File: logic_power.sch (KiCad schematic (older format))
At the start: 28 parts

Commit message: Huge schematic and documentation update
Signed-off-by: Patrick Rudolph <siro@das-labor.org>
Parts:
- removed C?: 2u2, symbol Device:C_Small
- removed D?: 6V8, symbol Device:D_Zener_Small
- removed D?: D_Schottky, symbol Device:D_Schottky
- removed Q?: MMBTA42, symbol Device:Q_NPN_BCE
- removed R?: 220k, symbol Device:R
- removed R?: 130, symbol Device:R
- removed T?: PA1528, symbol Device:Transformer_1P_2S
- added C? (x2): 10u, symbol Device:C_Small
- added D?: MBR2H200SF, Diode_SMD:D_SOD-123, symbol Device:D_Schottky
- added D?: BAT54T1G, Diode_SMD:D_SOD-123, symbol Device:D_Schottky
- added TR?: 7491199212, symbol Transformer:TRANSF6
- C?: value 100p -> 360p
- D?: value 8V1 -> BZT52B8V2; footprint (none) -> Diode_SMD:D_SOD-123
- D?: value D_Schottky -> BAT54T1G; footprint (none) -> Diode_SMD:D_SOD-123
- R?: value 68 -> 300k
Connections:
- net 12V: now also D?.1 (K)
- net 12V+_isolated: now also C?.1, C?.1
- net 12V-_isolated: now also C?.2, C?.2, TR?.7
- net GND: now also TR?.4, TR?.5; no longer C?.2
- net V_IN: now also C?.1, R?.2, TR?.1
- net at Q?.1 (D): now also D?.2 (A), TR?.2; no longer R?.2
- net at D?.2 (A): now also TR?.8
- net at R?.1: now also C?.2, D?.1 (K); no longer C?.1
- net V_BACKUP renamed V_SUPPLY
- new net: D?.2 (A), TR?.3, TR?.6
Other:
- note added: "Coutmin = (Ioutmax * 10) / (fsw * Vout_ripple)\n= (0,05A * 10) / (200e3 * 0,1)\n= 25uF"
- note added: "Csnub = (2 * Lleak * Ip ^2 * n ^2 ) / (Vout ^2)\n= (2 * 2.3e-6 * 0.32^2 * 0.33^2) / (12^2)\n= 356pF"
- note added: "Rclamp = (4 * Vr^2) / (Lleak * Ip ^2 * fsw)\n= 4 * 60^2 / (2.3e-6 * 0.32^2 * 200e3)\n= 14.4 / (2.3e-6 * 0.32^2 * 200)\n= 305k"
- note added: "Vin 20-60V\nN 1:0.29\nVout 12V\nIpri = 0.32A\nIsec = 0.100A\nLleak = 2.3 uH"
- moved on the sheet: C?, R?

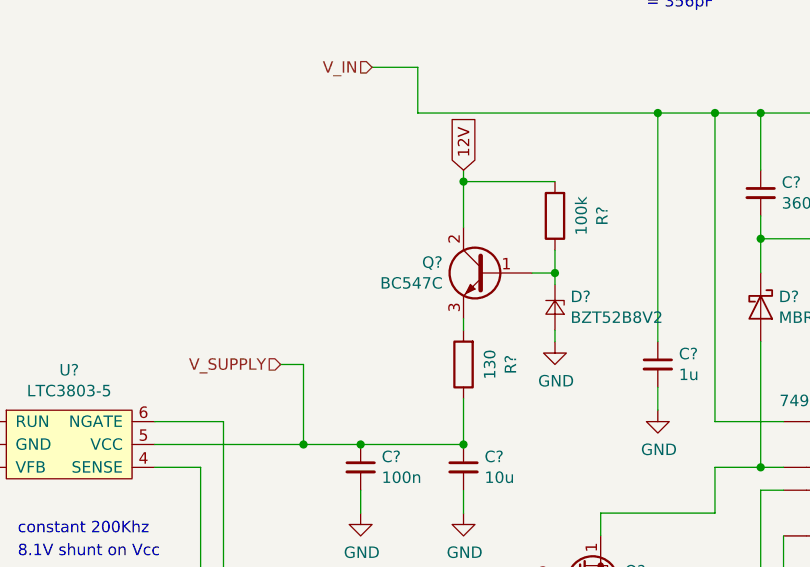
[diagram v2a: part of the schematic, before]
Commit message: Add more packages
Signed-off-by: Patrick Rudolph <siro@das-labor.org>
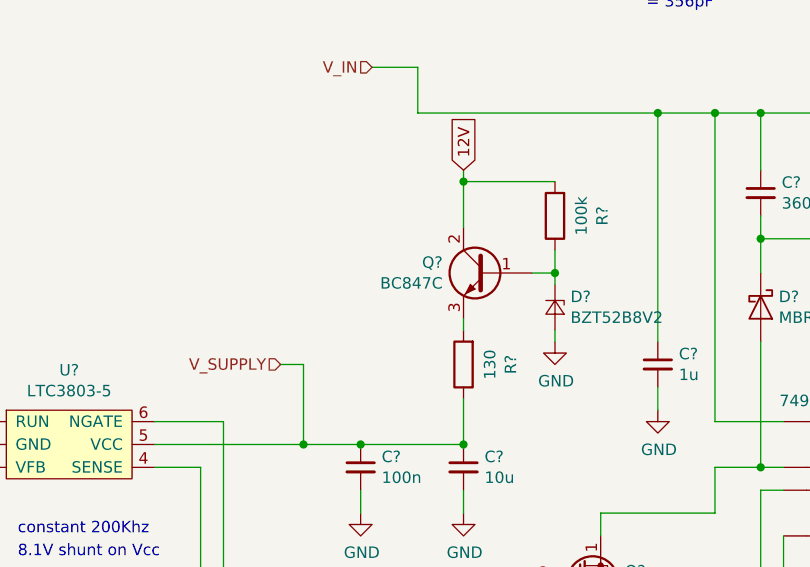
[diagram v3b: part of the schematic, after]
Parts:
- C? (x6): footprint (none) -> Capacitor_SMD:C_1206_3216Metric
- C? (x3): footprint (none) -> Capacitor_SMD:C_0603_1608Metric
- Q?: value BC547C -> BC847C; footprint (none) -> Package_TO_SOT_SMD:SOT-23
- R? (x6): footprint (none) -> Resistor_SMD:R_0603_1608Metric
- U?: footprint (none) -> Package_TO_SOT_SMD:SOT-23-6_Handsoldering
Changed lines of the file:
@@
 EESchema Schematic File Version 4
 LIBS:mppt_power-cache
-EELAYER 29 0
+EELAYER 30 0
 EELAYER END
 $Descr A4 11693 8268
@@
 F 0 "U?" H 3275 4025 50  0000 C CNN
 F 1 "LTC3803-5" H 3275 3934 50  0000 C CNN
-F 2 "" H 3250 3500 50  0001 C CNN
+F 2 "Package_TO_SOT_SMD:SOT-23-6_Handsoldering" H 3250 3500 50  0001 C CNN
 F 3 "https://www.analog.com/media/en/technical-documentation/data-sheets/38035fc.pdf" H 3250 3500 50  0001 C CNN
 	1    3250 3500
@@
 F 0 "C?" H 5092 3446 50  0000 L CNN
 F 1 "10u" H 5092 3355 50  0000 L CNN
-F 2 "" H 5000 3400 50  0001 C CNN
+F 2 "Capacitor_SMD:C_1206_3216Metric" H 5000 3400 50  0001 C CNN
 F 3 "~" H 5000 3400 50  0001 C CNN
 	1    5000 3400
@@
 F 0 "C?" H 4642 3446 50  0000 L CNN
 F 1 "100n" H 4642 3355 50  0000 L CNN
-F 2 "" H 4550 3400 50  0001 C CNN
+F 2 "Capacitor_SMD:C_0603_1608Metric" H 4550 3400 50  0001 C CNN
 F 3 "~" H 4550 3400 50  0001 C CNN
 	1    4550 3400
@@
 F 0 "R?" V 6493 2150 50  0000 C CNN
 F 1 "300k" V 6584 2150 50  0000 C CNN
-F 2 "" V 6630 2150 50  0001 C CNN
+F 2 "Resistor_SMD:R_0603_1608Metric" V 6630 2150 50  0001 C CNN
 F 3 "~" H 6700 2150 50  0001 C CNN
 	1    6700 2150
@@
 F 0 "C?" H 6392 2246 50  0000 L CNN
 F 1 "360p" H 6392 2155 50  0000 L CNN
-F 2 "" H 6300 2200 50  0001 C CNN
+F 2 "Capacitor_SMD:C_0603_1608Metric" H 6300 2200 50  0001 C CNN
 F 3 "~" H 6300 2200 50  0001 C CNN
 	1    6300 2200
@@
 F 0 "R?" V 4743 4150 50  0000 C CNN
 F 1 "4k7" V 4834 4150 50  0000 C CNN
-F 2 "" V 4880 4150 50  0001 C CNN
+F 2 "Resistor_SMD:R_0603_1608Metric" V 4880 4150 50  0001 C CNN
 F 3 "~" H 4950 4150 50  0001 C CNN
 	1    4950 4150
@@
 F 0 "C?" H 7692 3796 50  0000 L CNN
 F 1 "10u" H 7692 3705 50  0000 L CNN
-F 2 "" H 7600 3750 50  0001 C CNN
+F 2 "Capacitor_SMD:C_1206_3216Metric" H 7600 3750 50  0001 C CNN
 F 3 "~" H 7600 3750 50  0001 C CNN
 	1    7600 3750
@@
 F 0 "C?" H 8042 3796 50  0000 L CNN
 F 1 "10u" H 8042 3705 50  0000 L CNN
-F 2 "" H 7950 3750 50  0001 C CNN
+F 2 "Capacitor_SMD:C_1206_3216Metric" H 7950 3750 50  0001 C CNN
 F 3 "~" H 7950 3750 50  0001 C CNN
 	1    7950 3750
@@
 F 0 "C?" H 5942 2996 50  0000 L CNN
 F 1 "1u" H 5942 2905 50  0000 L CNN
-F 2 "" H 5850 2950 50  0001 C CNN
+F 2 "Capacitor_SMD:C_1206_3216Metric" H 5850 2950 50  0001 C CNN
 F 3 "~" H 5850 2950 50  0001 C CNN
 	1    5850 2950
@@
 F 0 "R?" V 7543 2800 50  0000 C CNN
 F 1 "680" V 7634 2800 50  0000 C CNN
-F 2 "" V 7680 2800 50  0001 C CNN
+F 2 "Resistor_SMD:R_0603_1608Metric" V 7680 2800 50  0001 C CNN
 F 3 "~" H 7750 2800 50  0001 C CNN
 	1    7750 2800
@@
 F 0 "C?" H 2142 3446 50  0000 L CNN
 F 1 "1n" H 2142 3355 50  0000 L CNN
-F 2 "" H 2050 3400 50  0001 C CNN
+F 2 "Capacitor_SMD:C_0603_1608Metric" H 2050 3400 50  0001 C CNN
 F 3 "~" H 2050 3400 50  0001 C CNN
 	1    2050 3400
@@
 F 0 "R?" V 2193 3200 50  0000 C CNN
 F 1 "22k" V 2284 3200 50  0000 C CNN
-F 2 "" V 2330 3200 50  0001 C CNN
+F 2 "Resistor_SMD:R_0603_1608Metric" V 2330 3200 50  0001 C CNN
 F 3 "~" H 2400 3200 50  0001 C CNN
 	1    2400 3200
@@
 P 5100 2550
 F 0 "Q?" H 5291 2596 50  0000 L CNN
-F 1 "BC547C" H 5291 2505 50  0000 L CNN
-F 2 "" H 5300 2650 50  0001 C CNN
+F 1 "BC847C" H 5291 2505 50  0000 L CNN
+F 2 "Package_TO_SOT_SMD:SOT-23" H 5300 2650 50  0001 C CNN
 F 3 "~" H 5100 2550 50  0001 C CNN
 	1    5100 2550
@@
 F 0 "R?" V 4793 2950 50  0000 C CNN
 F 1 "130" V 4884 2950 50  0000 C CNN
-F 2 "" V 4930 2950 50  0001 C CNN
+F 2 "Resistor_SMD:R_0603_1608Metric" V 4930 2950 50  0001 C CNN
 F 3 "~" H 5000 2950 50  0001 C CNN
 	1    5000 2950
@@
 F 0 "R?" V 5193 2300 50  0000 C CNN
 F 1 "100k" V 5284 2300 50  0000 C CNN
-F 2 "" V 5330 2300 50  0001 C CNN
+F 2 "Resistor_SMD:R_0603_1608Metric" V 5330 2300 50  0001 C CNN
 F 3 "~" H 5400 2300 50  0001 C CNN
 	1    5400 2300
@@
 F 0 "C?" H 8542 2796 50  0000 L CNN
 F 1 "10u" H 8542 2705 50  0000 L CNN
-F 2 "" H 8450 2750 50  0001 C CNN
+F 2 "Capacitor_SMD:C_1206_3216Metric" H 8450 2750 50  0001 C CNN
 F 3 "~" H 8450 2750 50  0001 C CNN
 	1    8450 2750
@@
 F 0 "C?" H 8192 2796 50  0000 L CNN
 F 1 "10u" H 8192 2705 50  0000 L CNN
-F 2 "" H 8100 2750 50  0001 C CNN
+F 2 "Capacitor_SMD:C_1206_3216Metric" H 8100 2750 50  0001 C CNN
 F 3 "~" H 8100 2750 50  0001 C CNN
 	1    8100 2750

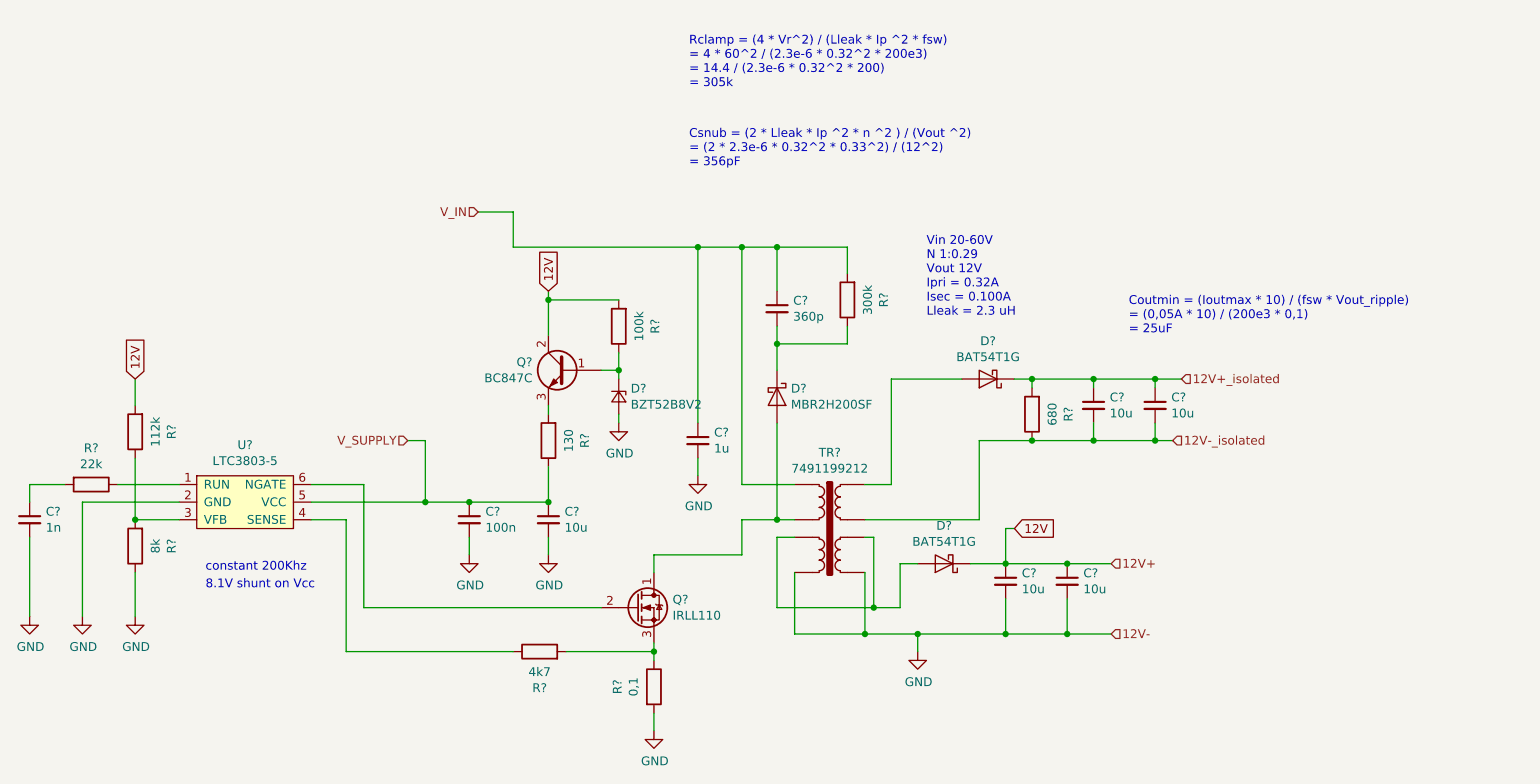
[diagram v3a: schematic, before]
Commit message: Split into more schematics, add more comments
Signed-off-by: Patrick Rudolph <siro@das-labor.org>
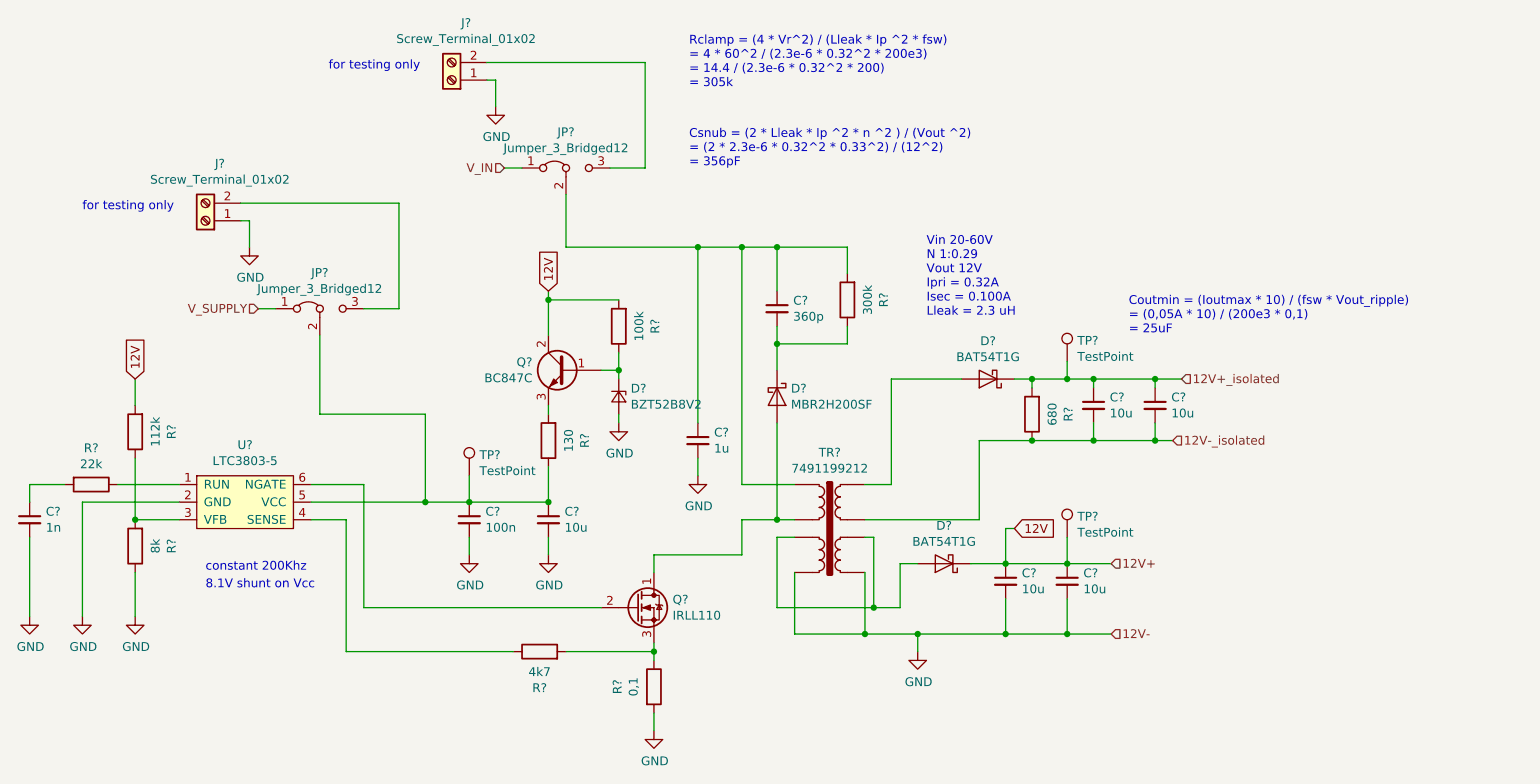
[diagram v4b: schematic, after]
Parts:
- added J? (x2): Screw_Terminal_01x02, symbol Connector:Screw_Terminal_01x02
- added JP? (x2): Jumper_3_Bridged12, symbol Jumper:Jumper_3_Bridged12
- added TP? (x3): TestPoint, symbol Connector:TestPoint
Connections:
- net 12V: now also TP?.1
- net 12V+_isolated: now also TP?.1
- net GND: now also J?.1 (Pin_1), J?.1 (Pin_1)
- net V_IN: now also JP?.1 (A); no longer C?.1, C?.1, R?.2, TR?.1
- net V_SUPPLY: now also JP?.1 (A); no longer C?.1, C?.1, R?.1, U?.5 (VCC)
- new net: C?.1, C?.1, JP?.2 (C), R?.2, TR?.1
- new net: C?.1, C?.1, JP?.2 (C), R?.1, TP?.1, U?.5 (VCC)
- new net: J?.2 (Pin_2), JP?.3 (B) (x2)
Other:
- note added: "for testing only"
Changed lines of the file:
@@
 $Descr A4 11693 8268
 encoding utf-8
-Sheet 2 3
+Sheet 2 5
 Title ""
 Date ""
@@
 Wire Wire Line
 	2350 3300 2350 3950
-Wire Wire Line
-	3650 3300 4300 3300
 Wire Wire Line
 	4550 3300 5000 3300
@@
 	7750 2650 7750 2600
 Connection ~ 7750 2600
-Text HLabel 4600 1650 0    50   Input ~ 0
+Text HLabel 4750 1400 0    50   Input ~ 0
 V_IN
-Wire Wire Line
-	4600 1650 4800 1650
-Wire Wire Line
-	4800 1650 4800 1850
-Wire Wire Line
-	4800 1850 5850 1850
 $Comp
 L Device:R R?
@@
 $EndComp
 Wire Wire Line
-	7750 2600 8100 2600
+	7750 2600 7950 2600
 Wire Wire Line
 	7750 2950 8100 2950
@@
 	-1   0    0    1
 $EndComp
-Text HLabel 4200 2950 0    50   Input ~ 0
+Text HLabel 3350 2200 0    50   Input ~ 0
 V_SUPPLY
-Wire Wire Line
-	4200 2950 4300 2950
-Wire Wire Line
-	4300 2950 4300 3300
+$Comp
+L Connector:TestPoint TP?
+U 1 1 5DA4B3AA
+P 4550 3150
+F 0 "TP?" H 4608 3268 50  0000 L CNN
+F 1 "TestPoint" H 4608 3177 50  0000 L CNN
+F 2 "" H 4750 3150 50  0001 C CNN
+F 3 "~" H 4750 3150 50  0001 C CNN
+	1    4550 3150
+	1    0    0    -1
+$EndComp
+$Comp
+L Connector:TestPoint TP?
+U 1 1 5DA4BF3C
+P 7950 3500
+F 0 "TP?" H 8008 3618 50  0000 L CNN
+F 1 "TestPoint" H 8008 3527 50  0000 L CNN
+F 2 "" H 8150 3500 50  0001 C CNN
+F 3 "~" H 8150 3500 50  0001 C CNN
+	1    7950 3500
+	1    0    0    -1
+$EndComp
+Wire Wire Line
+	7950 3500 7950 3650
+$Comp
+L Connector:TestPoint TP?
+U 1 1 5DA503D9
+P 7950 2500
+F 0 "TP?" H 8008 2618 50  0000 L CNN
+F 1 "TestPoint" H 8008 2527 50  0000 L CNN
+F 2 "" H 8150 2500 50  0001 C CNN
+F 3 "~" H 8150 2500 50  0001 C CNN
+	1    7950 2500
+	1    0    0    -1
+$EndComp
+Wire Wire Line
+	7950 2500 7950 2600
+Connection ~ 7950 2600
+Wire Wire Line
+	7950 2600 8100 2600
+Wire Wire Line
+	4550 3150 4550 3300
+$Comp
+L Jumper:Jumper_3_Bridged12 JP?
+U 1 1 5DA5817D
+P 3700 2200
+F 0 "JP?" H 3700 2404 50  0000 C CNN
+F 1 "Jumper_3_Bridged12" H 3700 2313 50  0000 C CNN
+F 2 "" H 3700 2200 50  0001 C CNN
+F 3 "~" H 3700 2200 50  0001 C CNN
+	1    3700 2200
+	1    0    0    -1
+$EndComp
+Wire Wire Line
+	3650 3300 4300 3300
+Wire Wire Line
+	3350 2200 3450 2200
+Wire Wire Line
+	3700 2350 3700 2800
+Wire Wire Line
+	3700 2800 4300 2800
+Wire Wire Line
+	4300 2800 4300 3300
 Connection ~ 4300 3300
 Wire Wire Line
 	4300 3300 4550 3300
+$Comp
+L Connector:Screw_Terminal_01x02 J?
+U 1 1 5DA67559
+P 3050 1700
+F 0 "J?" H 2968 1375 50  0000 C CNN
+F 1 "Screw_Terminal_01x02" H 2968 1466 50  0000 C CNN
+F 2 "" H 3050 1700 50  0001 C CNN
+F 3 "~" H 3050 1700 50  0001 C CNN
+	1    3050 1700
+	-1   0    0    1
+$EndComp
+$Comp
+L power:GND #PWR?
+U 1 1 5DA681B7
+P 3300 1850
+AR Path="/5DA681B7" Ref="#PWR?"  Part="1"
+AR Path="/5DAB7E1F/5DA681B7" Ref="#PWR?"  Part="1"
+F 0 "#PWR?" H 3300 1600 50  0001 C CNN
+F 1 "GND" H 3305 1677 50  0000 C CNN
+F 2 "" H 3300 1850 50  0001 C CNN
+F 3 "" H 3300 1850 50  0001 C CNN
+	1    3300 1850
+	1    0    0    -1
+$EndComp
+Wire Wire Line
+	3250 1700 3300 1700
+Wire Wire Line
+	3300 1700 3300 1850
+Wire Wire Line
+	3250 1600 4150 1600
+Wire Wire Line
+	4150 1600 4150 2200
+Wire Wire Line
+	4150 2200 3950 2200
+Text Notes 2350 1650 0    50   ~ 0
+for testing only
+$Comp
+L Jumper:Jumper_3_Bridged12 JP?
+U 1 1 5D8A6170
+P 5100 1400
+F 0 "JP?" H 5100 1604 50  0000 C CNN
+F 1 "Jumper_3_Bridged12" H 5100 1513 50  0000 C CNN
+F 2 "" H 5100 1400 50  0001 C CNN
+F 3 "~" H 5100 1400 50  0001 C CNN
+	1    5100 1400
+	1    0    0    -1
+$EndComp
+Wire Wire Line
+	4750 1400 4850 1400
+$Comp
+L Connector:Screw_Terminal_01x02 J?
+U 1 1 5D8A6177
+P 4450 900
+F 0 "J?" H 4368 575 50  0000 C CNN
+F 1 "Screw_Terminal_01x02" H 4368 666 50  0000 C CNN
+F 2 "" H 4450 900 50  0001 C CNN
+F 3 "~" H 4450 900 50  0001 C CNN
+	1    4450 900
+	-1   0    0    1
+$EndComp
+$Comp
+L power:GND #PWR?
+U 1 1 5D8A617D
+P 4700 1050
+AR Path="/5D8A617D" Ref="#PWR?"  Part="1"
+AR Path="/5DAB7E1F/5D8A617D" Ref="#PWR?"  Part="1"
+F 0 "#PWR?" H 4700 800 50  0001 C CNN
+F 1 "GND" H 4705 877 50  0000 C CNN
+F 2 "" H 4700 1050 50  0001 C CNN
+F 3 "" H 4700 1050 50  0001 C CNN
+	1    4700 1050
+	1    0    0    -1
+$EndComp
+Wire Wire Line
+	4650 900  4700 900
+Wire Wire Line
+	4700 900  4700 1050
+Wire Wire Line
+	4650 800  5550 800
+Wire Wire Line
+	5550 800  5550 1400
+Wire Wire Line
+	5550 1400 5350 1400
+Text Notes 3750 850  0    50   ~ 0
+for testing only
+Wire Wire Line
+	5100 1550 5100 1850
+Wire Wire Line
+	5100 1850 5850 1850
 $EndSCHEMATC
